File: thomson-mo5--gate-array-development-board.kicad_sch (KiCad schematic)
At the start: 0 parts

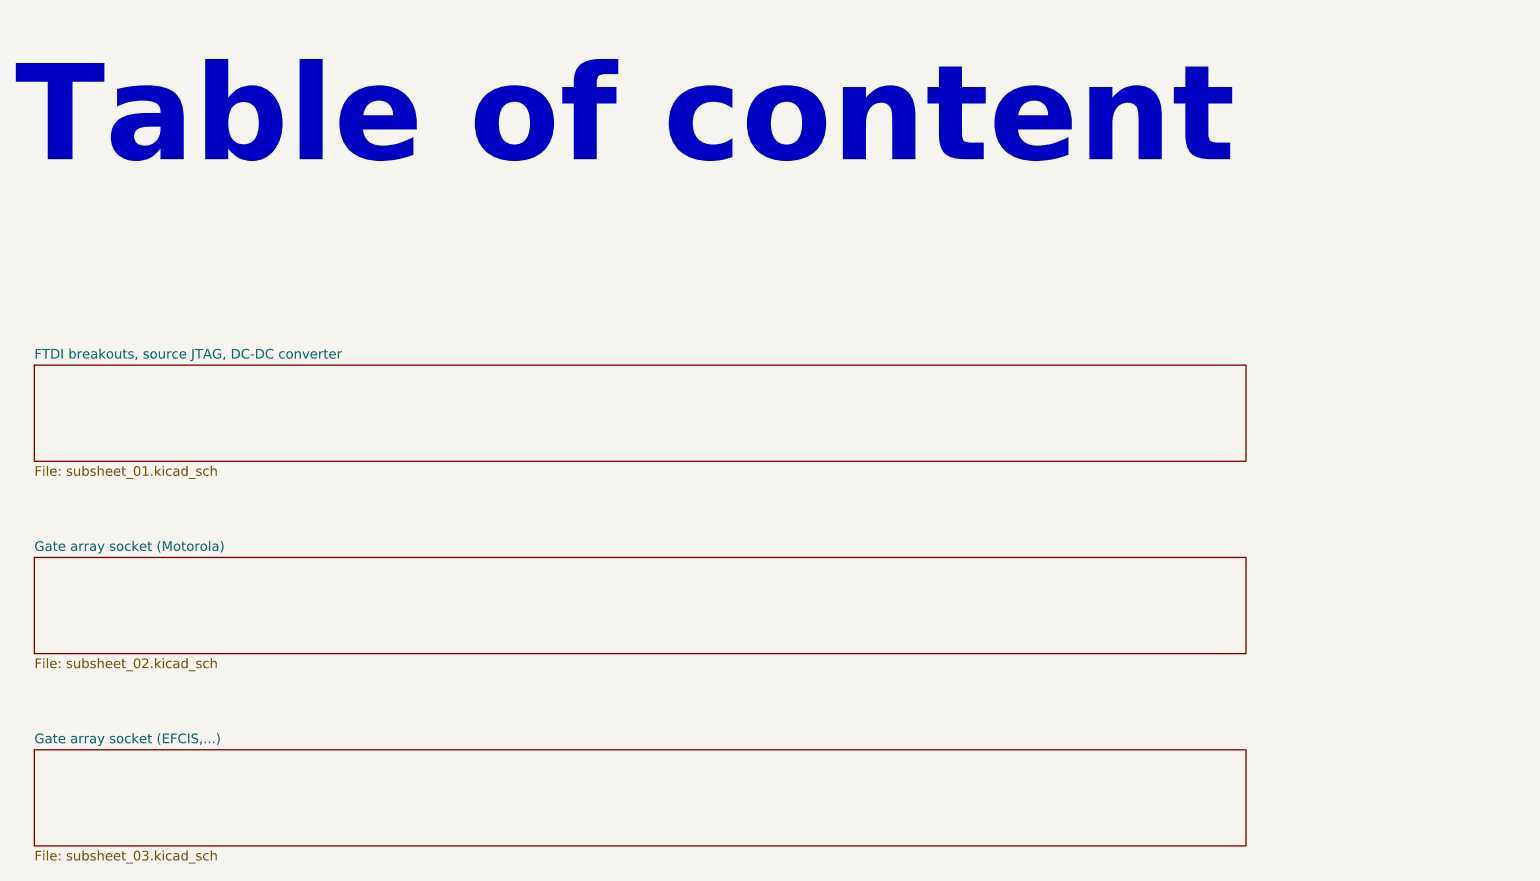
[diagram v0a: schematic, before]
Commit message: Patched release : fixed table of content in schematics
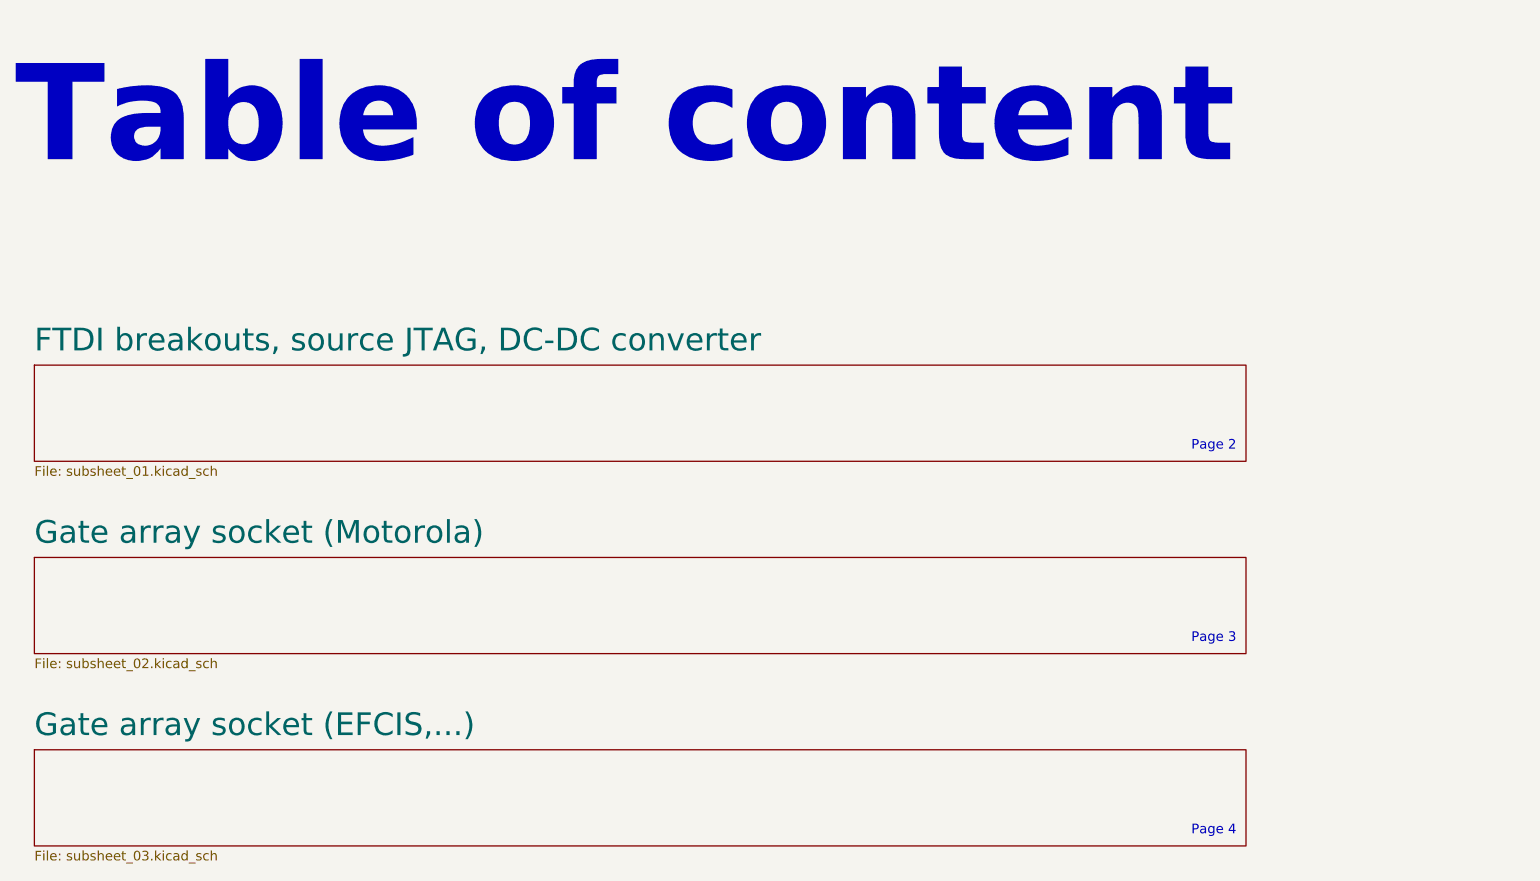
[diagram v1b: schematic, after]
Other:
- note added: "Page 2"
- note added: "Page 3"
- note added: "Page 4"
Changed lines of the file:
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@@
     (title "Thomson MO5 — Gate array development board")
     (date "2025-07-13")
-    (rev "v1.0.0")
+    (rev "v1.0.1")
     (company "Sporniket.com")
+  )
+  (text "Page 2" (at 184.15 74.93 0)
+    (effects (font (size 1.27 1.27)) (justify right bottom))
   )
   (text "Table of content" (at 22.86 38.1 0)
     (effects (font (size 12.7 12.7) (thickness 2.54) bold) (justify left bottom))
   )
+  (text "Page 4" (at 184.15 125.73 0)
+    (effects (font (size 1.27 1.27)) (justify right bottom))
+  )
+  (text "Page 3" (at 184.15 100.33 0)
+    (effects (font (size 1.27 1.27)) (justify right bottom))
+  )
   (sheet (at 25.4 114.3) (size 160.02 12.7) (fields_autoplaced)
     (stroke (width 0.1524) (type solid))
     (fill (color 0 0 0 0.0000))
-    (property "Sheetname" "Gate array socket (EFCIS,...)" (at 25.4 113.5884 0)
-      (effects (font (size 1.27 1.27)) (justify left bottom))
+    (property "Sheetname" "Gate array socket (EFCIS,...)" (at 25.4 112.7234 0)
+      (effects (font (size 3 3)) (justify left bottom))
     )
     (property "Sheetfile" "subsheet_03.kicad_sch" (at 25.4 127.5846 0)
@@
     (stroke (width 0.1524) (type solid))
     (fill (color 0 0 0 0.0000))
-    (property "Sheetname" "Gate array socket (Motorola)" (at 25.4 88.1884 0)
-      (effects (font (size 1.27 1.27)) (justify left bottom))
+    (property "Sheetname" "Gate array socket (Motorola)" (at 25.4 87.3234 0)
+      (effects (font (size 3 3)) (justify left bottom))
     )
     (property "Sheetfile" "subsheet_02.kicad_sch" (at 25.4 102.1846 0)
@@
     (stroke (width 0.1524) (type solid))
     (fill (color 0 0 0 0.0000))
-    (property "Sheetname" "FTDI breakouts, source JTAG, DC-DC converter" (at 25.4 62.7884 0)
-      (effects (font (size 1.27 1.27)) (justify left bottom))
+    (property "Sheetname" "FTDI breakouts, source JTAG, DC-DC converter" (at 25.4 61.9234 0)
+      (effects (font (size 3 3)) (justify left bottom))
     )
     (property "Sheetfile" "subsheet_01.kicad_sch" (at 25.4 76.7846 0)
